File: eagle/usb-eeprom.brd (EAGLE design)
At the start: 160 x 100 mm, 0 parts

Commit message: Add PIC18(L)F45K50 symbol
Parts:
- added C1: (no value), rcl:C0805
- added D1: (no value), led:CHIPLED_0805
- added R1: (no value), rcl:R0805
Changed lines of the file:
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@@
 <setting verticaltext="up"/>
 </settings>
-<grid distance="0.05" unitdist="inch" unit="inch" style="lines" multiple="1" display="no" altdistance="0.025" altunitdist="inch" altunit="inch"/>
+<grid distance="0.05" unitdist="inch" unit="inch" style="lines" multiple="1" display="yes" altdistance="0.025" altunitdist="inch" altunit="inch"/>
 <layers>
 <layer number="1" name="Top" color="4" fill="1" visible="yes" active="yes"/>
@@
 </autorouter>
 <elements>
+<element name="C1" library="rcl" package="C0805" value="" x="2.54" y="-3.81"/>
+<element name="R1" library="rcl" package="R0805" value="" x="2.54" y="-8.89"/>
+<element name="D1" library="led" package="CHIPLED_0805" value="" x="-3.81" y="-7.62">
+<attribute name="PARTNO" value="APT2012SGC" x="-3.81" y="-7.62" size="1.778" layer="27" display="off"/>
+</element>
 </elements>
 <signals>

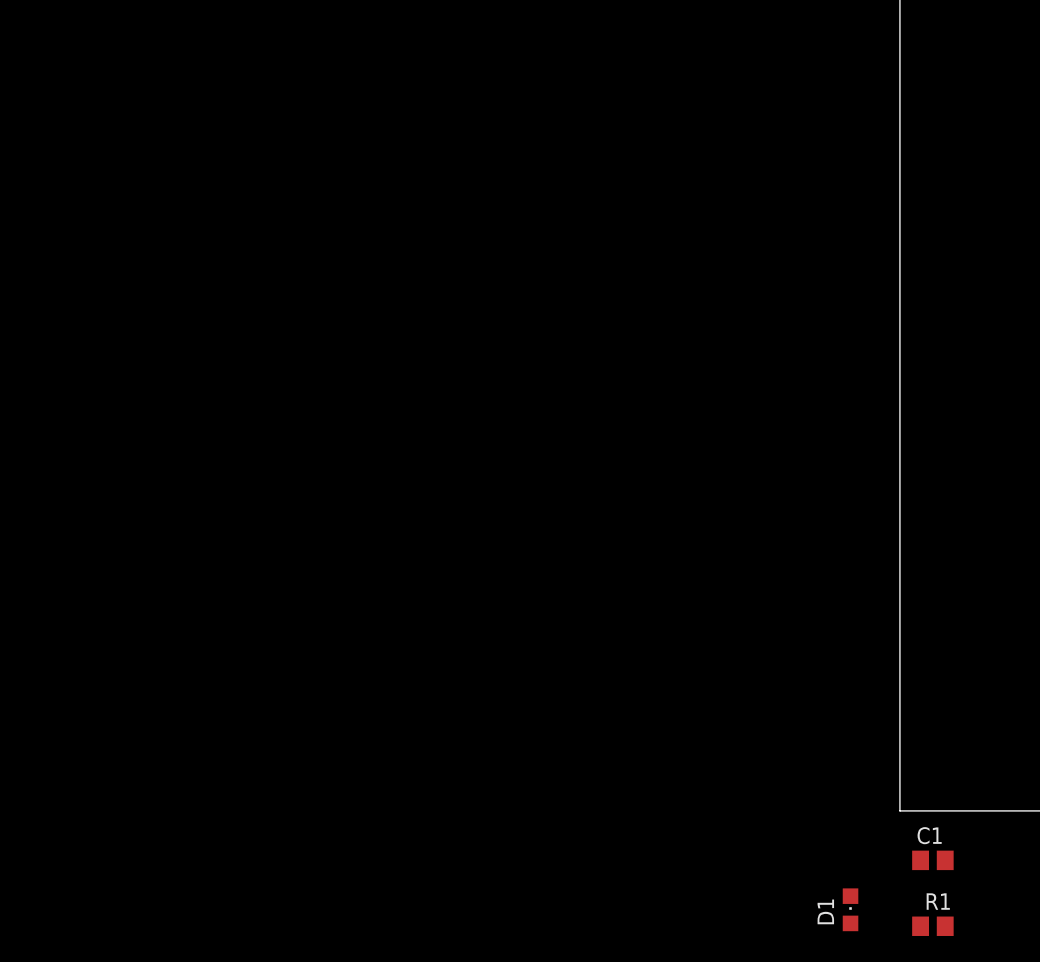
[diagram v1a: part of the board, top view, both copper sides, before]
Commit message: Update schematic; generate BOM
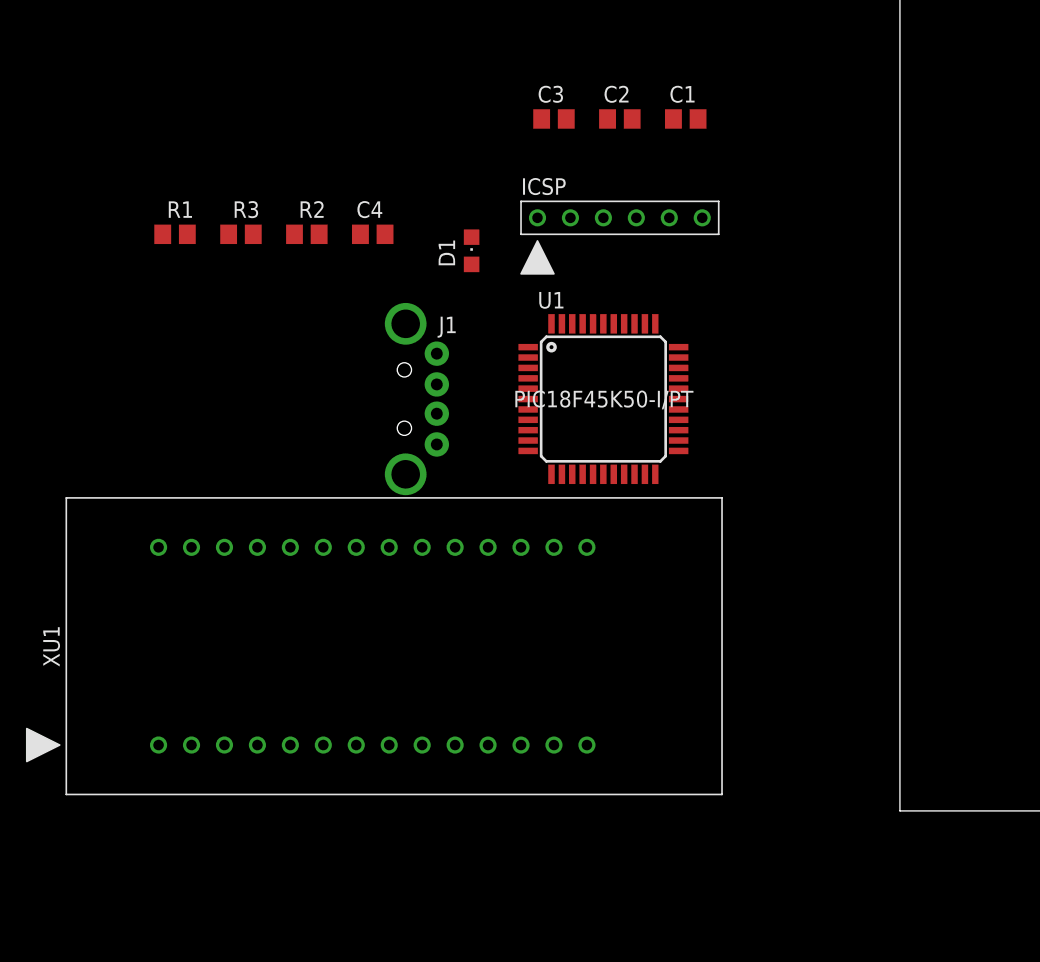
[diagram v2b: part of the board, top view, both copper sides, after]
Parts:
- added C2, C3: .1uF, rcl:C0805
- added C4: .22uF, rcl:C0805
- added ICSP: ICSP, usb-eeprom:ICSP
- added J1: USBA, usb-eeprom:USBA
- added R2, R3: 10K, rcl:R0805
- added U1: PIC18F45K50-I/PT, usb-eeprom:TQFP44
- added XU1: 28CXXX-ZIF, usb-eeprom:ZIF28
- C1: value (none) -> .1uF
- D1: value (none) -> GREEN
- R1: value (none) -> 150
- moved R1 79.1 mm to (-55.9, 44.5)
- moved C1 60.2 mm to (-16.5, 53.3)
- moved D1 58.6 mm to (-33.0, 43.2)
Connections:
- new net +5V: C1.1, C2.1, C3.1, ICSP.2, J1.1, R1.2, R2.2, R3.2, U1.28, U1.7, XU1.28
- new net A0: U1.19, XU1.10
- new net A1: U1.20, XU1.9
- new net A10: U1.10, XU1.21
- new net A11: U1.11, XU1.23
- new net A12: U1.14, XU1.2
- new net A13: U1.32, XU1.26
- new net A14: U1.35, XU1.1
- new net A2: U1.21, XU1.8
- new net A3: U1.22, XU1.7
- new net A4: U1.23, XU1.6
- new net A5: U1.24, XU1.5
- new net A6: U1.31, XU1.4
- new net A7: U1.30, XU1.3
- new net A8: U1.8, XU1.25
- new net A9: U1.9, XU1.24
- new net D0: U1.38, XU1.11
- new net D1: U1.39, XU1.12
- new net D2: U1.40, XU1.13
- new net D3: U1.41, XU1.15
- new net D4: U1.2, XU1.16
- new net D5: U1.3, XU1.17
- new net D6: U1.4, XU1.18
- new net D7: U1.5, XU1.19
- new net GND: C1.2, C2.2, C3.2, C4.2, D1.C, ICSP.3, J1.4, J1.5, J1.6, U1.29, U1.6, XU1.14
- new net N$1: ICSP.1, R2.1, U1.18
- new net N$10: D1.A, R1.1
- new net N$2: ICSP.5, U1.16
- new net N$3: ICSP.4, U1.17
- new net N$4: C4.1, U1.37
- new net N$5: R3.1, U1.25, XU1.20
- new net N$6: J1.2, U1.42
- new net N$7: J1.3, U1.43
- new net N$8: U1.26, XU1.22
- new net N$9: U1.27, XU1.27

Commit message: Initial PCB layout
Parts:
- added LOGO: OSHW_LOGO_FILLX0200-NT, ohw-logo:OSHW_FILLX200_NOTEXT
- D1: value GREEN -> BLUE
- R1: value 150 -> 100
- moved XU1 96.0 mm to (55.3, 11.4)
- moved C4 78.2 mm to (27.3, 5.71), flipped to the bottom, turned to 135 degrees
- moved R1 70.1 mm to (10.2, 21.0)
- moved R3 69.3 mm to (10.2, 11.4), turned to 180 degrees
- moved C3 65.0 mm to (27.3, 17.1), flipped to the bottom, turned to 225 degrees
- moved C1 64.0 mm to (38.7, 21.0), flipped to the bottom, turned to 180 degrees
- moved R2 62.5 mm to (10.2, 16.5), turned to 180 degrees
- moved C2 60.6 mm to (15.9, 5.71), flipped to the bottom, turned to 225 degrees
- moved ICSP 49.8 mm to (21.6, 21.0)
- moved U1 48.9 mm to (21.6, 11.4), turned to 225 degrees
- moved J1 45.8 mm to (3.00, 11.4)
- moved D1 43.6 mm to (4.45, 21.0), turned to 90 degrees
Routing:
- net N$5: track 0.00 -> 54.0 mm, vias 0 -> 4
- net D3: track 0.00 -> 50.1 mm
- net A0: track 0.00 -> 50.0 mm, vias 0 -> 1
- net A1: track 0.00 -> 47.5 mm, vias 0 -> 1
- net A4: track 0.00 -> 45.6 mm
- net A2: track 0.00 -> 45.6 mm, vias 0 -> 1
- net D2: track 0.00 -> 44.7 mm
- net D4: track 0.00 -> 43.8 mm
- net A3: track 0.00 -> 43.2 mm, vias 0 -> 1
- net D1: track 0.00 -> 42.5 mm
- net N$8: track 0.00 -> 42.4 mm, vias 0 -> 1
- net D5: track 0.00 -> 41.5 mm
- net A5: track 0.00 -> 41.0 mm
- net D0: track 0.00 -> 40.6 mm
- net D6: track 0.00 -> 39.3 mm
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- added copper zone on layer 1, net +5V
- added copper zone on layer 16, net GND
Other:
- board size 160 x 100 mm -> 82.2 x 22.9 mm
- board text added: "28Cxxx EEPROM Programmer"
- board text added: "REV 1.00"
- board text added: "http://github.com/sstallion/usb-eeprom"

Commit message: Replace D1 with SML0805 package
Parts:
- D1: device led:CHIPLED_0805 -> led:SML0805
- turned D1 to 0 degrees
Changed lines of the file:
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@@
 </element>
 <element name="ICSP" library="usb-eeprom" package="ICSP" value="ICSP" x="21.59" y="20.955" smashed="yes">
-<attribute name="MFG" value="N/A" x="21.59" y="20.955" size="1.778" layer="27" display="off"/>
-<attribute name="MFG_PN" value="N/A" x="21.59" y="20.955" size="1.778" layer="27" display="off"/>
-<attribute name="MOUSER_PN" value="N/A" x="21.59" y="20.955" size="1.778" layer="27" display="off"/>
-<attribute name="NOTES" value="N/A" x="21.59" y="20.955" size="1.778" layer="27" display="off"/>
 <attribute name="NAME" x="29.21" y="19.05" size="1.27" layer="25" font="vector" align="top-right"/>
 </element>
@@
 <attribute name="NAME" x="10.16" y="19.685" size="0.762" layer="25" font="vector" align="top-center"/>
 </element>
-<element name="D1" library="led" package="CHIPLED_0805" value="BLUE" x="4.445" y="20.955" smashed="yes" rot="R90">
-<attribute name="MOUSER_PN" value="604-APT2012QBC/D" x="47.625" y="53.975" size="1.778" layer="27" rot="R90" display="off"/>
-<attribute name="MFG" value="Kingbright" x="47.625" y="53.975" size="1.778" layer="27" rot="R90" display="off"/>
-<attribute name="NOTES" value="3.3V 20mA" x="47.625" y="53.975" size="1.778" layer="27" rot="R90" display="off"/>
-<attribute name="MFG_PN" value="APT2012QBC/D" x="47.625" y="53.975" size="1.778" layer="27" rot="R90" display="off"/>
-<attribute name="NAME" x="4.445" y="19.685" size="0.762" layer="25" font="vector" align="top-center"/>
+<element name="D1" library="led" package="SML0805" value="BLUE" x="4.445" y="20.955" smashed="yes">
+<attribute name="MOUSER_PN" value="604-APT2012QBC/D" x="37.465" y="-22.225" size="1.778" layer="27" display="off"/>
+<attribute name="MFG" value="Kingbright" x="37.465" y="-22.225" size="1.778" layer="27" display="off"/>
+<attribute name="NOTES" value="3.3V 20mA" x="37.465" y="-22.225" size="1.778" layer="27" display="off"/>
+<attribute name="MFG_PN" value="APT2012QBC/D" x="37.465" y="-22.225" size="1.778" layer="27" display="off"/>
+<attribute name="NAME" x="3.175" y="20.955" size="0.762" layer="25" font="vector" rot="R270" align="top-center"/>
 </element>
 <element name="C1" library="rcl" package="C0805" value=".1uF" x="38.735" y="20.955" smashed="yes" rot="MR180">

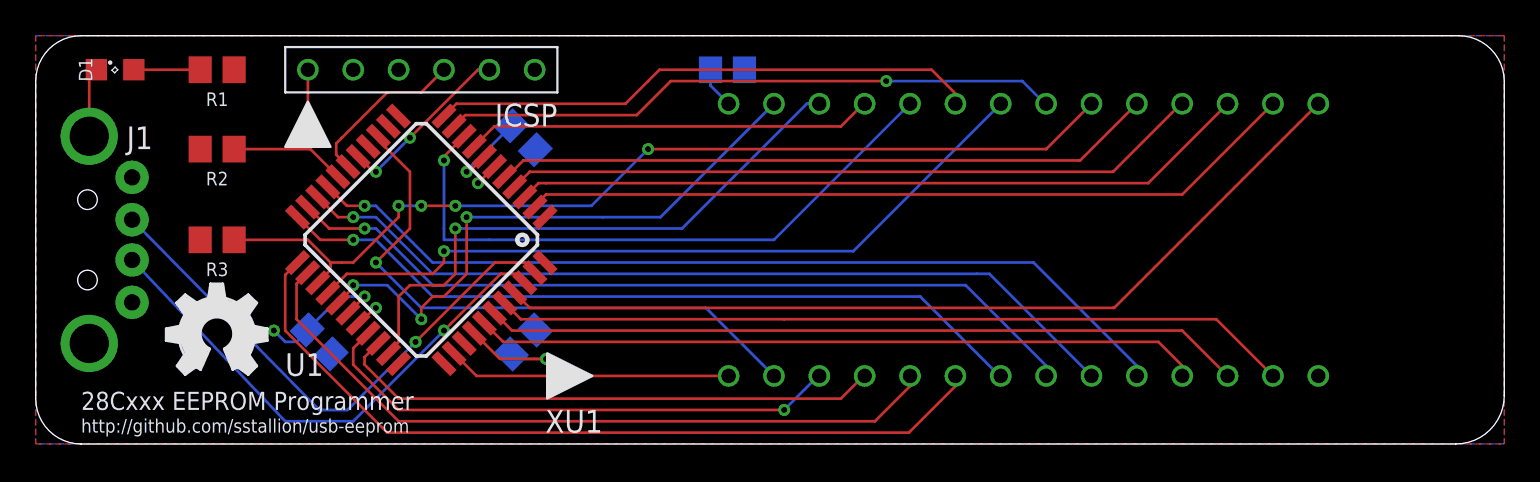
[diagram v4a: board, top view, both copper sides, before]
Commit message: Cosmetic fixes; REV 1.01 layout
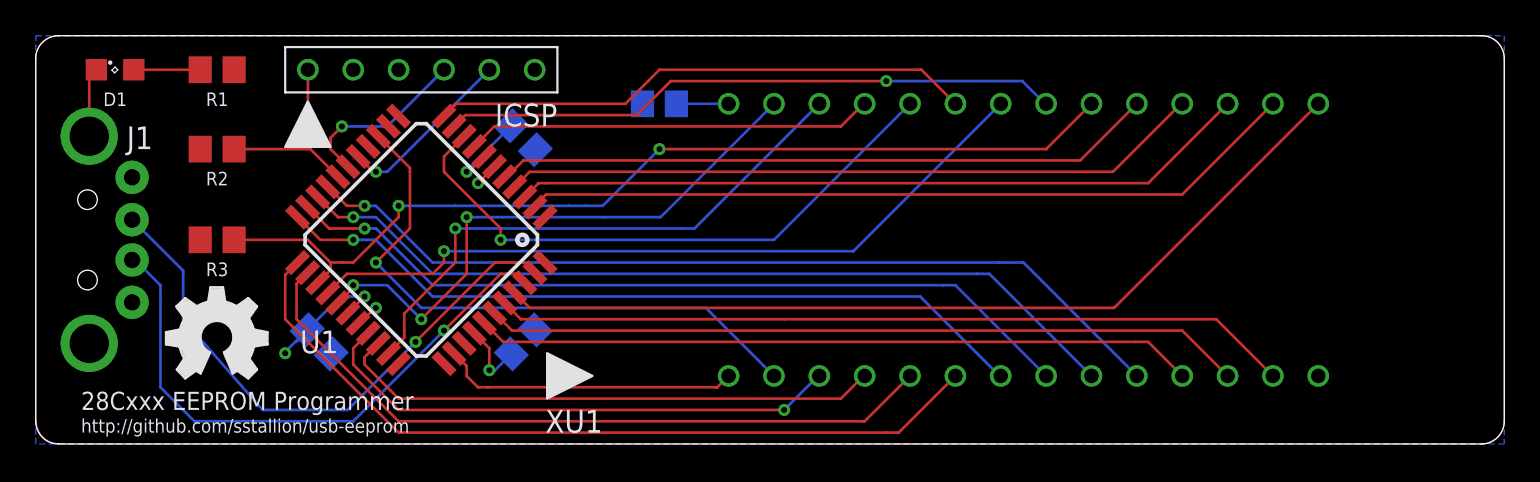
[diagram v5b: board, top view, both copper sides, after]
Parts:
- removed LOGO: OSHW_LOGO_FILLX0200-NT, ohw-logo:OSHW_FILLX200_NOTEXT
- added U$1: OSHW, usb-eeprom:OSHW
- moved C1 4.26 mm to (34.9, 19.1), turned to 0 degrees
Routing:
- net N$6: track 29.5 -> 32.7 mm
- net N$4: track 6.67 -> 4.43 mm
- net A9: track 35.5 -> 33.7 mm
- net N$7: track 30.7 -> 32.4 mm
- net A13: track 32.9 -> 31.9 mm
- net +5V: track 15.0 -> 15.9 mm
- net A14: track 15.9 -> 16.7 mm
- net A4: track 45.6 -> 44.9 mm
- net N$3: track 9.31 -> 9.95 mm, vias 0 -> 1
- net N$5: vias 4 -> 2
- net N$2: vias 2 -> 1
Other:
- outline, holes or cut-outs redrawn
- board text added: "REV 1.01"
- board text removed: "REV 1.00"

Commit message: Update documentation
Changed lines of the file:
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@@
 <attribute name="MOUSER_PN" value="579-PIC18F45K50-I/PT" x="-17.0251" y="17.71618125" size="1.778" layer="27" rot="R225" display="off"/>
 <attribute name="MFG" value="Microchip Technology" x="-17.0251" y="17.71618125" size="1.778" layer="27" rot="R225" display="off"/>
-<attribute name="NOTES" value="48MHz 32KB FLASH/RAM" x="-17.0251" y="17.71618125" size="1.778" layer="27" rot="R225" display="off"/>
+<attribute name="NOTES" value="48MHz 32KB FLASH 2KB RAM" x="-17.0251" y="17.71618125" size="1.778" layer="27" rot="R225" display="off"/>
 <attribute name="MFG_PN" value="PIC18F45K50-I/PT" x="-17.0251" y="17.71618125" size="1.778" layer="27" rot="R225" display="off"/>
 <attribute name="NAME" x="15.875" y="5.715" size="1.27" layer="25" font="vector" align="center"/>
@@
 <contactref element="C3" pad="2"/>
 <polygon width="0.4064" layer="16">
-<vertex x="0" y="22.86"/>
-<vertex x="82.2325" y="22.86"/>
-<vertex x="82.2325" y="0"/>
-<vertex x="0" y="0"/>
+<vertex x="82.2325" y="21.59"/>
+<vertex x="82.2325" y="1.27" curve="-90"/>
+<vertex x="80.9625" y="0"/>
+<vertex x="1.27" y="0" curve="-90"/>
+<vertex x="0" y="1.27"/>
+<vertex x="0" y="21.59" curve="-90"/>
+<vertex x="1.27" y="22.86"/>
+<vertex x="80.9625" y="22.86" curve="-90"/>
 </polygon>
 <wire x1="3.395" y1="20.955" x2="2.9972" y2="20.5572" width="0.1524" layer="1"/>
